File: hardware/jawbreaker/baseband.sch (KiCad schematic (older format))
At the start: 120 parts, among them P1 RX_SMA, P10 CONN_3, P11 1V8, P12 CONN_3, P13 CONN_3, P14 CONN_3, P15 CONN_3, P2 TX_SMA, P3 SPI, P4 VCC, P5 ADC/DAC, P6 XCVR_CTL, P7 CLOCK_CTL, P8 GSG-SMA-CONN, P9 CONN_2, T1 RX_BALUN, T2 TX_BALUN, U1 MAX5864, U2 MAX2837, U3 SI5351C, X1 GSG-XTAL4PIN

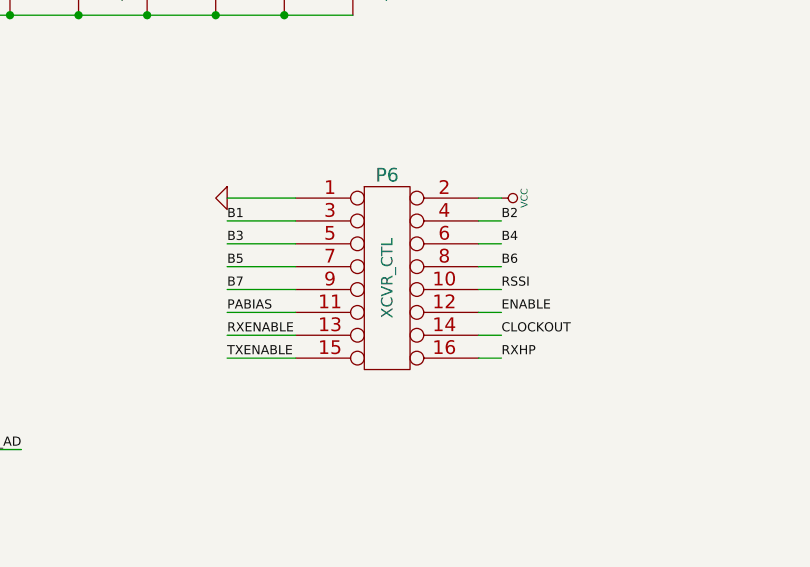
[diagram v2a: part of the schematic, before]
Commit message: removed XCVR_CTL signals that we never used
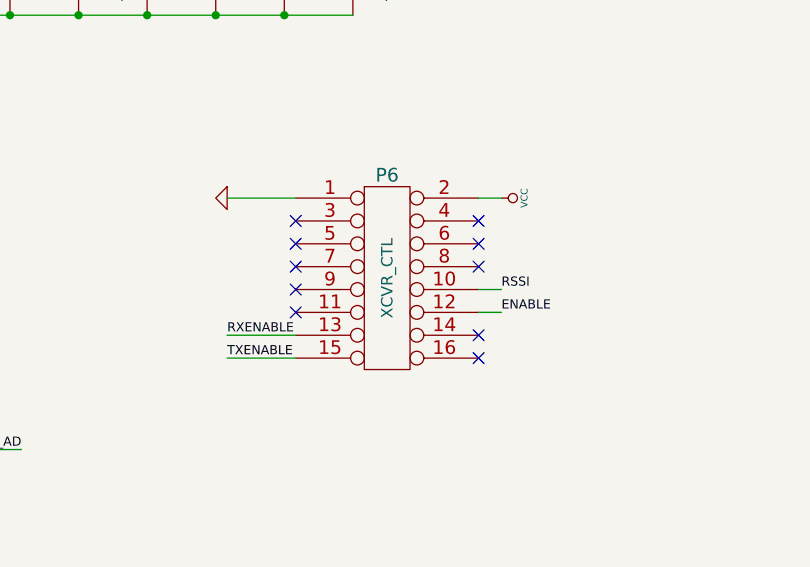
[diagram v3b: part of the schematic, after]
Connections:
- net B1: no longer P6.3
- net B2: no longer P6.4
- net B3: no longer P6.5
- net B4: no longer P6.6
- net B5: no longer P6.7
- net B6: no longer P6.8
- net B7: no longer P6.9
- net CLOCKOUT: no longer P6.14
- net PABIAS: no longer P6.11
- net RXHP: no longer P6.16
- no-connect marks 1 -> 11
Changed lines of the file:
@@
-EESchema Schematic File Version 2  date Thu Aug 23 23:42:08 2012
+EESchema Schematic File Version 2  date Thu Aug 23 23:50:26 2012
 LIBS:power
 LIBS:device
@@
 Comment4 ""
 $EndDescr
+NoConn ~ 4400 2800
+NoConn ~ 5200 2900
+NoConn ~ 5200 3000
+NoConn ~ 5200 2600
+NoConn ~ 5200 2500
+NoConn ~ 5200 2400
+NoConn ~ 4400 2700
+NoConn ~ 4400 2600
+NoConn ~ 4400 2500
+NoConn ~ 4400 2400
 Text Label 4700 9000 1    40   ~ 0
 VDDOB
@@
 Connection ~ 1950 9150
 Wire Wire Line
-	5200 2900 5300 2900
-Wire Wire Line
 	4100 2300 4400 2300
 Wire Wire Line
@@
 Wire Wire Line
 	5200 2700 5300 2700
-Wire Wire Line
-	5200 2500 5300 2500
-Wire Wire Line
-	4400 2800 4100 2800
-Wire Wire Line
-	4400 2600 4100 2600
-Wire Wire Line
-	4400 2400 4100 2400
 Wire Wire Line
 	1150 2700 1450 2700
@@
 	1150 2600 1450 2600
 Wire Wire Line
-	4400 2500 4100 2500
-Wire Wire Line
-	4400 2700 4100 2700
-Wire Wire Line
-	5200 2400 5300 2400
-Wire Wire Line
-	5200 2600 5300 2600
-Wire Wire Line
 	5200 2800 5300 2800
 Wire Wire Line
@@
 Wire Wire Line
 	4400 2900 4100 2900
-Wire Wire Line
-	5200 3000 5300 3000
 Wire Wire Line
 	5150 4500 5050 4500
@@
 	0    1    1    0
 $EndComp
-Text Label 5300 3000 0    40   ~ 0
-RXHP
 Text Label 4100 3000 0    40   ~ 0
 TXENABLE
@@
 	1    0    0    -1
 $EndComp
-Text Label 5300 2900 0    40   ~ 0
-CLOCKOUT
-Text Label 4100 2800 0    40   ~ 0
-PABIAS
 Text Label 5300 2800 0    40   ~ 0
 ENABLE
-Text Label 4100 2700 0    40   ~ 0
-B7
 Text Label 5300 2700 0    40   ~ 0
 RSSI
-Text Label 4100 2600 0    40   ~ 0
-B5
-Text Label 5300 2600 0    40   ~ 0
-B6
-Text Label 4100 2500 0    40   ~ 0
-B3
-Text Label 5300 2500 0    40   ~ 0
-B4
-Text Label 4100 2400 0    40   ~ 0
-B1
-Text Label 5300 2400 0    40   ~ 0
-B2
 $Comp
 L GND #PWR9

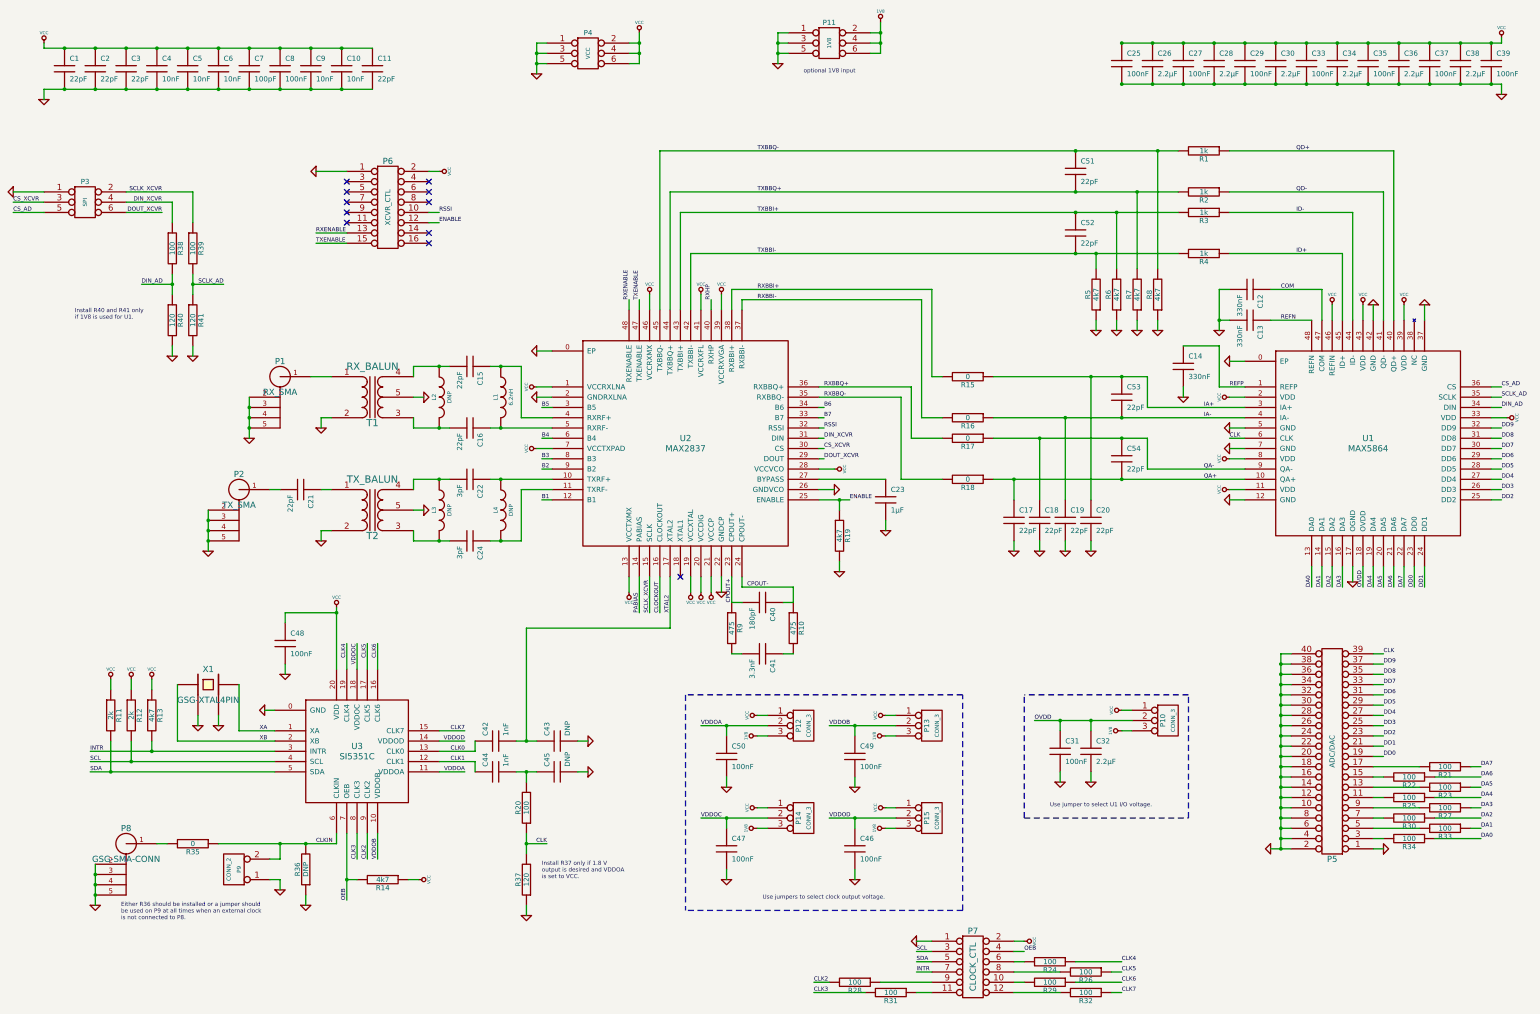
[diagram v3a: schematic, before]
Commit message: xcvr CLOCKOUT test point
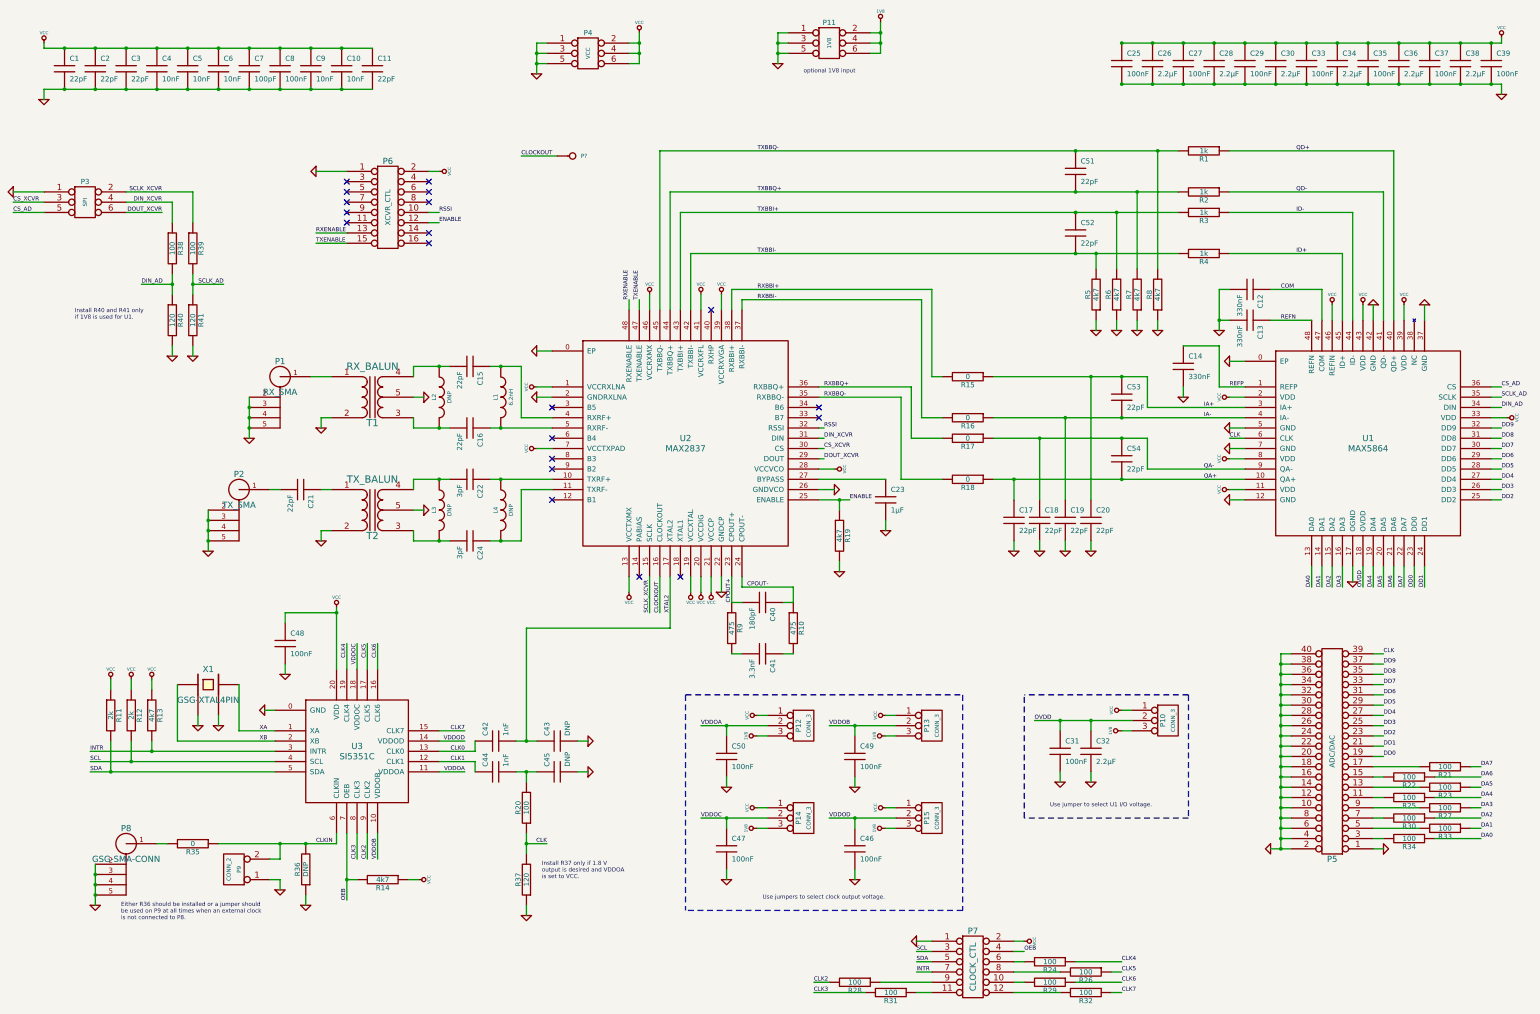
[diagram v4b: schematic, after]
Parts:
- added P?: CONN_1, symbol CONN_1
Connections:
- net CLOCKOUT: now also P?.1
- net B1: no longer names the net of U2.12 (B1)
- net B2: no longer names the net of U2.9 (B2)
- net B3: no longer names the net of U2.8 (B3)
- net B4: no longer names the net of U2.6 (B4)
- net B5: no longer names the net of U2.3 (B5)
- net B6: no longer names the net of U2.34 (B6)
- net B7: no longer names the net of U2.33 (B7)
- net PABIAS: no longer names the net of U2.14 (PABIAS)
- net RXHP: no longer names the net of U2.40 (RXHP)
- no-connect marks 11 -> 20

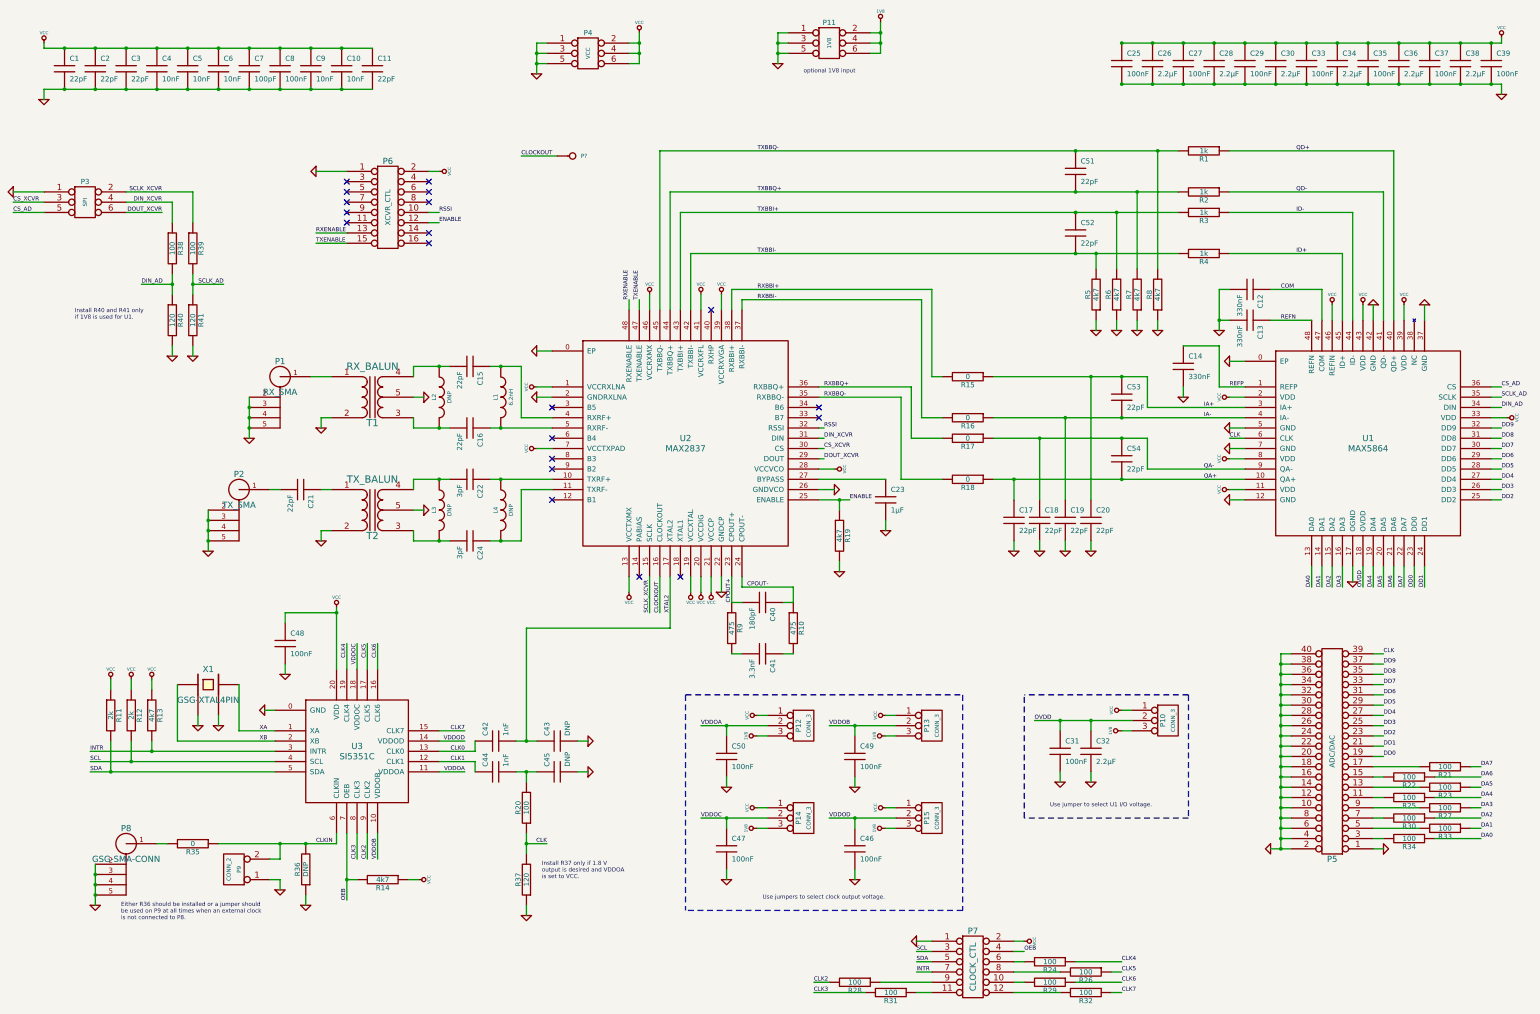
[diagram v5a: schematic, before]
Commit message: global labels for DA* and DD*, 39 ohm series resistors
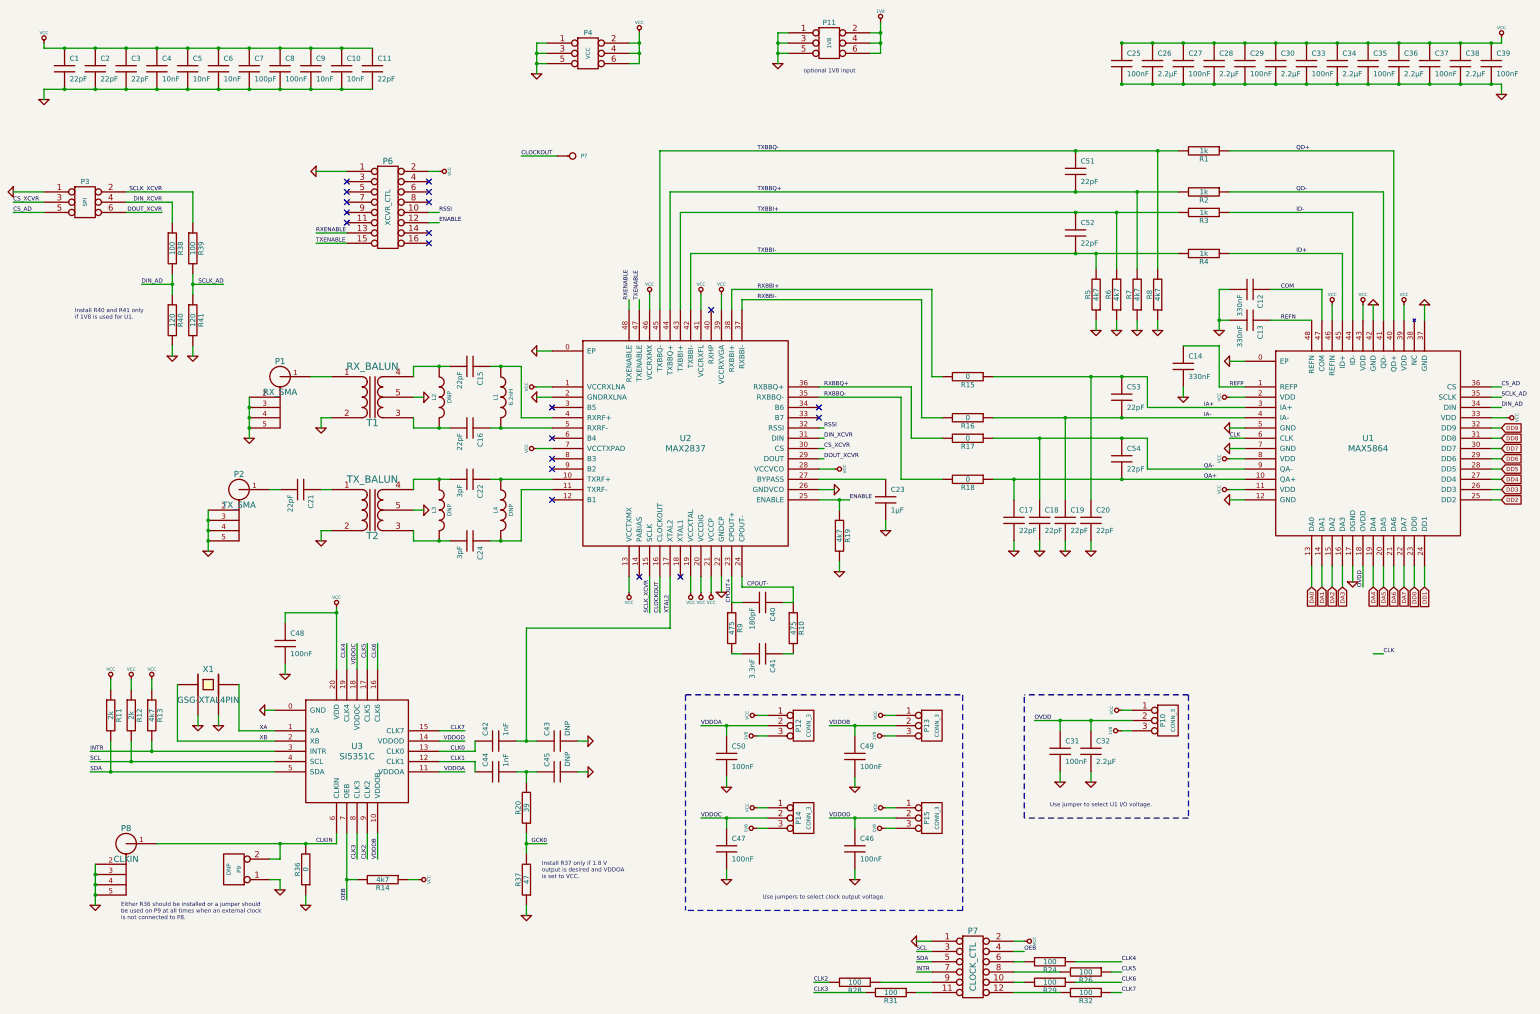
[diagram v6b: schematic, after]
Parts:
- removed P5: ADC/DAC, symbol CONN_20X2
- removed R21, R22, R23, R25, R27, R30, R33, R34: 100, symbol R
- removed R35: 0, symbol R
- P8: value GSG-SMA-CONN -> CLKIN; Note (none) -> DNP
- P9: value CONN_2 -> DNP
- R20: value 100 -> 39
- R36: value DNP -> 0
- R37: value 120 -> 47; Note (none) -> DNP
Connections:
- net CLK: no longer R20.1, R37.2
- net CLKIN: now also P8.1 (RF)
- new net GCK0: R20.1, R37.2

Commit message: more of the same
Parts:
- removed R24, R26, R29, R31, R32: 100, symbol R
- added R? (x5): 39, symbol R
- P9: value DNP -> CLKIN_JMP; Note (none) -> DNP
- R28: value 100 -> 39
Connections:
- net CLK is gone; now on net GCK0: U1.6 (CLK)
- net CLK3: now also R?.2
- net CLK4: now also R?.1
- net CLK5: now also R?.1
- net CLK6: now also R?.1
- net CLK7: now also R?.1
- net at P7.10: now also R?.2
- net at P7.11: now also R?.1
- net at P7.12: now also R?.2
- net at P7.6 (P6): now also R?.2
- net at P7.8 (P8): now also R?.2
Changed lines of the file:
@@
-EESchema Schematic File Version 2  date Fri Aug 24 00:31:47 2012
+EESchema Schematic File Version 2  date Fri Aug 24 00:37:44 2012
 LIBS:power
 LIBS:device
@@
 Comment4 ""
 $EndDescr
+$Comp
+L R R?
+U 1 1 50372135
+P 11600 10300
+F 0 "R?" V 11680 10300 50  0000 C CNN
+F 1 "39" V 11600 10300 50  0000 C CNN
+	1    11600 10300
+	0    1    1    0
+$EndComp
+$Comp
+L R R?
+U 1 1 50372131
+P 11250 10200
+F 0 "R?" V 11330 10200 50  0000 C CNN
+F 1 "39" V 11250 10200 50  0000 C CNN
+	1    11250 10200
+	0    1    1    0
+$EndComp
+$Comp
+L R R?
+U 1 1 5037212F
+P 11600 10100
+F 0 "R?" V 11680 10100 50  0000 C CNN
+F 1 "39" V 11600 10100 50  0000 C CNN
+	1    11600 10100
+	0    1    1    0
+$EndComp
+$Comp
+L R R?
+U 1 1 5037212C
+P 11250 10000
+F 0 "R?" V 11330 10000 50  0000 C CNN
+F 1 "39" V 11250 10000 50  0000 C CNN
+	1    11250 10000
+	0    1    1    0
+$EndComp
+$Comp
+L R R?
+U 1 1 5037212A
+P 9700 10300
+F 0 "R?" V 9780 10300 50  0000 C CNN
+F 1 "39" V 9700 10300 50  0000 C CNN
+	1    9700 10300
+	0    1    1    0
+$EndComp
+Text GLabel 6250 8850 2    40   Input ~ 0
+GCK0
+Text GLabel 13000 4900 0    40   Input ~ 0
+GCK0
 Text GLabel 14700 6350 3    40   Input ~ 0
 DA7
@@
 Wire Wire Line
 	9100 10200 8950 10200
-Wire Wire Line
-	14400 7000 14500 7000
 Connection ~ 4000 8850
 Wire Wire Line
@@
 Connection ~ 2900 3400
 Wire Wire Line
-	6350 8850 6150 8850
+	6250 8850 6150 8850
 Connection ~ 6150 8850
 Wire Wire Line
@@
 	1    0    0    -1
 $EndComp
-Text Label 6350 8850 2    40   ~ 0
-GCK0
-Text Label 14500 7000 0    40   ~ 0
-CLK
 Text Notes 1750 3750 0    40   ~ 0
 Install R40 and R41 only\nif 1V8 is used for U1.
@@
 F 0 "R37" V 6230 9200 50  0000 C CNN
 F 1 "47" V 6150 9200 50  0000 C CNN
-F 4 "DNP" V 6150 9200 60  0001 C CNN "Note"
+F 4 "DNP" V 6350 9200 60  0000 C CNN "Note"
 	1    6150 9200
 	-1   0    0    1
@@
 P 9350 10200
 F 0 "R28" V 9430 10200 50  0000 C CNN
-F 1 "100" V 9350 10200 50  0000 C CNN
+F 1 "39" V 9350 10200 50  0000 C CNN
 	1    9350 10200
-	0    1    1    0
-$EndComp
-$Comp
-L R R31
-U 1 1 4F5D6F5C
-P 9700 10300
-F 0 "R31" V 9780 10300 50  0000 C CNN
-F 1 "100" V 9700 10300 50  0000 C CNN
-	1    9700 10300
 	0    1    1    0
 $EndComp
@@
 Text Label 11950 10000 0    40   ~ 0
 CLK4
-$Comp
-L R R32
-U 1 1 4F5D6F3C
-P 11600 10300
-F 0 "R32" V 11680 10300 50  0000 C CNN
-F 1 "100" V 11600 10300 50  0000 C CNN
-	1    11600 10300
-	0    1    1    0
-$EndComp
-$Comp
-L R R26
-U 1 1 4F5D6F34
-P 11600 10100
-F 0 "R26" V 11680 10100 50  0000 C CNN
-F 1 "100" V 11600 10100 50  0000 C CNN
-	1    11600 10100
-	0    1    1    0
-$EndComp
-$Comp
-L R R29
-U 1 1 4F5D6F31
-P 11250 10200
-F 0 "R29" V 11330 10200 50  0000 C CNN
-F 1 "100" V 11250 10200 50  0000 C CNN
-	1    11250 10200
-	0    1    1    0
-$EndComp
-$Comp
-L R R24
-U 1 1 4F5D6F1B
-P 11250 10000
-F 0 "R24" V 11330 10000 50  0000 C CNN
-F 1 "100" V 11250 10000 50  0000 C CNN
-	1    11250 10000
-	0    1    1    0
-$EndComp
 $Comp
 L GND #PWR53
@@
 P 3300 9100
 F 0 "P9" V 3250 9100 40  0000 C CNN
-F 1 "DNP" V 3350 9100 40  0000 C CNN
+F 1 "CLKIN_JMP" V 3350 9100 40  0000 C CNN
+F 4 "DNP" H 3500 9100 60  0000 C CNN "Note"
 	1    3300 9100
 	-1   0    0    1
@@
 F 0 "P8" H 2250 9000 60  0000 C CNN
 F 1 "CLKIN" H 2250 8700 60  0000 C CNN
-F 4 "DNP" H 2250 8850 60  0001 C CNN "Note"
+F 4 "DNP" H 2000 8800 60  0000 C CNN "Note"
 	1    2250 8850
 	1    0    0    -1
@@
 	0    -1   -1   0
 $EndComp
-Text Label 13000 4900 0    40   ~ 0
-CLK
 $Comp
 L GND #PWR44

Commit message: global labels for xcvr control
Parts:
- removed P6: XCVR_CTL, symbol CONN_8X2
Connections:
- net ENABLE renamed XCVR_EN
- no-connect marks 20 -> 10
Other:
- moved on the sheet: C23, R19
